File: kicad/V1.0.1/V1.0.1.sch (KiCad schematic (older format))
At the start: 20 parts, among them IC1 OPA2134P, U1 TLE2426CP

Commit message: Started to include libraries and sort out names to link to PCB
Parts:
- IC1: footprint V1.0.1:AKAFUGU_DIL-8 -> V1.0.1:DIL-8; symbol AKAFUGU_OPA2134P -> OPA2134P
- JACK-IN9, JACK-OUT9: footprint V1.0.1:AKAFUGU_STX3100 -> V1.0.1:STX3100; symbol AKAFUGU_STEREOJACK -> STEREOJACK
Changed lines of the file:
@@
 $EndComp
 $Comp
-L AKAFUGU_GND #GND01
+L GND #GND01
 U 1 1 58DE8183
 P 5200 3450
@@
 $EndComp
 $Comp
-L AKAFUGU_GND #GND02
+L GND #GND02
 U 1 1 58DE81E7
 P 5200 4350
@@
 $EndComp
 $Comp
-L AKAFUGU_OPA2134P IC1
+L OPA2134P IC1
 U 1 1 58DE82AF
 P 4600 5350
 F 0 "IC1" H 4700 5575 70  0000 L BNN
 F 1 "OPA2134P" H 4699 5150 70  0000 L BNN
-F 2 "V1.0.1:AKAFUGU_DIL-8" H 4590 5140 65  0001 L TNN
+F 2 "V1.0.1:DIL-8" H 4590 5140 65  0001 L TNN
 F 3 "" H 4600 5350 60  0001 C CNN
 	1    4600 5350
@@
 $EndComp
 $Comp
-L AKAFUGU_OPA2134P IC1
+L OPA2134P IC1
 U 2 1 58DE8313
 P 3200 2150
 F 0 "IC1" H 3300 2375 70  0000 L BNN
 F 1 "OPA2134P" H 3299 1950 70  0000 L BNN
-F 2 "V1.0.1:AKAFUGU_DIL-8" H 3190 1940 65  0001 L TNN
+F 2 "V1.0.1:DIL-8" H 3190 1940 65  0001 L TNN
 F 3 "" H 3200 2150 60  0001 C CNN
 	2    3200 2150
@@
 $EndComp
 $Comp
-L AKAFUGU_STEREOJACK JACK-IN9
+L STEREOJACK JACK-IN9
 U 1 1 58DE83DB
 P 5700 3050
 F 0 "JACK-IN9" H 5400 3200 70  0000 L BNN
 F 1 "STEREOJACK" H 5400 2650 70  0000 L BNN
-F 2 "V1.0.1:AKAFUGU_STX3100" H 5690 2840 65  0001 L TNN
+F 2 "V1.0.1:STX3100" H 5690 2840 65  0001 L TNN
 F 3 "" H 5700 3050 60  0001 C CNN
 	1    5700 3050
@@
 $EndComp
 $Comp
-L AKAFUGU_STEREOJACK JACK-OUT9
+L STEREOJACK JACK-OUT9
 U 1 1 58DE84A3
 P 5700 3950
 F 0 "JACK-OUT9" H 5400 4100 70  0000 L BNN
 F 1 "STEREOJACK" H 5400 3550 70  0000 L BNN
-F 2 "V1.0.1:AKAFUGU_STX3100" H 5690 3740 65  0001 L TNN
+F 2 "V1.0.1:STX3100" H 5690 3740 65  0001 L TNN
 F 3 "" H 5700 3950 60  0001 C CNN
 	1    5700 3950

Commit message: Corrected Schematic errors
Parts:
- renumbered 9V9 to 9V1, C1V+9 to C1V+1, C1V-9 to C1V-1, C4 to C2, C2L9 to C2L1, C2R9 to C2R1, JACK-IN9 to JACK-IN1, JACK-OUT9 to JACK-OUT1, R3L9 to R3L1, R3R9 to R3R1, R4L9 to R4L1, R4R9 to R4R1, R5L9 to R5L1, R5R9 to R5R1, R6L9 to R6L1, R6R9 to R6R1
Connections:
- net labels added: INPUT_L, INPUT_R, OUTPUT_L, OUTPUT_R
- wire segments 45 -> 48
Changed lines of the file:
@@
 EESchema Schematic File Version 2
 LIBS:V1.0.1
-LIBS:V1.0.1-cache
 EELAYER 25 0
 EELAYER END
@@
 Gain = 6
 $Comp
-L BATTERY_AB9V 9V9
+L BATTERY_AB9V 9V1
 U 1 1 58DE7C6F
 P 7950 5550
-F 0 "9V9" H 7725 5675 70  0000 L BNN
+F 0 "9V1" H 7725 5675 70  0000 L BNN
 F 1 "AB9V" H 7725 5350 70  0000 L BNN
 F 2 "V1.0.1:BATTERY_AB9V" H 7725 5350 70  0001 L BNN
@@
 $EndComp
 $Comp
-L CAPACITOR-WIMA_C2.5_2 C1V+9
+L CAPACITOR-WIMA_C2.5_2 C1V+1
 U 1 1 58DE7DFF
 P 10050 5250
-F 0 "C1V+9" H 10110 5265 70  0000 L BNN
+F 0 "C1V+1" H 10110 5265 70  0000 L BNN
 F 1 "0.068uF" H 10110 5065 70  0000 L BNN
 F 2 "V1.0.1:CAPACITOR-WIMA_C2.5-2" H 10040 5040 65  0001 L TNN
@@
 $EndComp
 $Comp
-L CAPACITOR-WIMA_C2.5_2 C1V-9
+L CAPACITOR-WIMA_C2.5_2 C1V-1
 U 1 1 58DE7EC7
 P 10050 5750
-F 0 "C1V-9" H 10110 5765 70  0000 L BNN
+F 0 "C1V-1" H 10110 5765 70  0000 L BNN
 F 1 "0.068uF" H 10110 5565 70  0000 L BNN
 F 2 "V1.0.1:CAPACITOR-WIMA_C2.5-2" H 10040 5540 65  0001 L TNN
@@
 $EndComp
 $Comp
-L CAPACITOR-WIMA_C5_5 C2L9
+L CAPACITOR-WIMA_C5_5 C2L1
 U 1 1 58DE7F8F
 P 4300 2050
-F 0 "C2L9" H 4360 2065 70  0000 L BNN
+F 0 "C2L1" H 4360 2065 70  0000 L BNN
 F 1 "0.1uF" H 4360 1865 70  0000 L BNN
 F 2 "V1.0.1:CAPACITOR-WIMA_C5B5" H 4290 1840 65  0001 L TNN
@@
 $EndComp
 $Comp
-L CAPACITOR-WIMA_C5_5 C2R9
+L CAPACITOR-WIMA_C5_5 C2R1
 U 1 1 58DE8057
 P 3500 5250
-F 0 "C2R9" H 3560 5265 70  0000 L BNN
+F 0 "C2R1" H 3560 5265 70  0000 L BNN
 F 1 "0.1uF" H 3560 5065 70  0000 L BNN
 F 2 "V1.0.1:CAPACITOR-WIMA_C5B5" H 3490 5040 65  0001 L TNN
@@
 $EndComp
 $Comp
-L CAPACITOR-WIMA_C5_2.5 C4
+L CAPACITOR-WIMA_C5_2.5 C2
 U 1 1 58DE811F
 P 9650 5850
-F 0 "C4" H 9710 5864 70  0000 L BNN
+F 0 "C2" H 9710 5864 70  0000 L BNN
 F 1 "1uF" H 9709 5665 70  0000 L BNN
 F 2 "V1.0.1:CAPACITOR-WIMA_C5B2.5" H 9640 5640 65  0001 L TNN
 F 3 "" H 9650 5850 60  0001 C CNN
 	1    9650 5850
-	1    0    0    -1
-$EndComp
-$Comp
-L GND #GND01
-U 1 1 58DE8183
-P 5200 3450
-F 0 "#GND01" H 5100 3350 70  0001 L BNN
-F 1 "GND" H 5100 3350 70  0000 L BNN
-F 2 "" H 5200 3450 60  0001 C CNN
-F 3 "" H 5200 3450 60  0001 C CNN
-	1    5200 3450
-	1    0    0    -1
-$EndComp
-$Comp
-L GND #GND02
-U 1 1 58DE81E7
-P 5200 4350
-F 0 "#GND02" H 5100 4250 70  0001 L BNN
-F 1 "GND" H 5100 4250 70  0000 L BNN
-F 2 "" H 5200 4350 60  0001 C CNN
-F 3 "" H 5200 4350 60  0001 C CNN
-	1    5200 4350
 	1    0    0    -1
 $EndComp
@@
 $EndComp
 $Comp
-L STEREOJACK JACK-IN9
+L STEREOJACK JACK-IN1
 U 1 1 58DE83DB
 P 5700 3050
-F 0 "JACK-IN9" H 5400 3200 70  0000 L BNN
+F 0 "JACK-IN1" H 5400 3200 70  0000 L BNN
 F 1 "STEREOJACK" H 5400 2650 70  0000 L BNN
 F 2 "V1.0.1:STX3100" H 5690 2840 65  0001 L TNN
@@
 $EndComp
 $Comp
-L STEREOJACK JACK-OUT9
+L STEREOJACK JACK-OUT1
 U 1 1 58DE84A3
 P 5700 3950
-F 0 "JACK-OUT9" H 5400 4100 70  0000 L BNN
+F 0 "JACK-OUT1" H 5400 4100 70  0000 L BNN
 F 1 "STEREOJACK" H 5400 3550 70  0000 L BNN
 F 2 "V1.0.1:STX3100" H 5690 3740 65  0001 L TNN
@@
 $EndComp
 $Comp
-L SUPPLY1_V+ #P+03
+L SUPPLY1_V+ #P+2
 U 1 1 58DE8507
 P 4500 4950
-F 0 "#P+03" V 4400 4850 70  0001 L BNN
+F 0 "#P+2" V 4400 4850 70  0001 L BNN
 F 1 "V+" V 4400 4850 70  0000 L BNN
 F 2 "" H 4500 4950 60  0001 C CNN
@@
 $EndComp
 $Comp
-L SUPPLY1_V+ #P+04
+L SUPPLY1_V+ #P+1
 U 1 1 58DE856B
 P 10150 4850
-F 0 "#P+04" V 10050 4750 70  0001 L BNN
+F 0 "#P+1" V 10050 4750 70  0001 L BNN
 F 1 "V+" V 10050 4750 70  0000 L BNN
 F 2 "" H 10150 4850 60  0001 C CNN
@@
 $EndComp
 $Comp
-L SUPPLY1_V- #P-05
+L SUPPLY1_V- #P-1
 U 1 1 58DE85CF
 P 4500 5750
-F 0 "#P-05" V 4300 5850 70  0001 R TNN
+F 0 "#P-1" V 4300 5850 70  0001 R TNN
 F 1 "V-" V 4300 5850 70  0000 R TNN
 F 2 "" H 4500 5750 60  0001 C CNN
@@
 $EndComp
 $Comp
-L SUPPLY1_V- #P-06
+L SUPPLY1_V- #P-2
 U 1 1 58DE8633
 P 10150 6250
-F 0 "#P-06" V 9950 6350 70  0001 R TNN
+F 0 "#P-2" V 9950 6350 70  0001 R TNN
 F 1 "V-" V 9950 6350 70  0000 R TNN
 F 2 "" H 10150 6250 60  0001 C CNN
@@
 $EndComp
 $Comp
-L RESISTOR_R-EU_0207_2V R3L9
+L RESISTOR_R-EU_0207_2V R3L1
 U 1 1 58DE86FB
 P 3900 2350
-F 0 "R3L9" H 3750 2409 70  0000 L BNN
+F 0 "R3L1" H 3750 2409 70  0000 L BNN
 F 1 "100k" H 3750 2220 70  0000 L BNN
 F 2 "V1.0.1:RESISTOR_0207_2V" H 3890 2140 65  0001 L TNN
@@
 $EndComp
 $Comp
-L RESISTOR_R-EU_0207_2V R3R9
+L RESISTOR_R-EU_0207_2V R3R1
 U 1 1 58DE87C3
 P 3900 5550
-F 0 "R3R9" H 3750 5609 70  0000 L BNN
+F 0 "R3R1" H 3750 5609 70  0000 L BNN
 F 1 "100k" H 3750 5420 70  0000 L BNN
 F 2 "V1.0.1:RESISTOR_0207_2V" H 3890 5340 65  0001 L TNN
@@
 $EndComp
 $Comp
-L RESISTOR_R-EU_0207_2V R4L9
+L RESISTOR_R-EU_0207_2V R4L1
 U 1 1 58DE888B
 P 3600 3150
-F 0 "R4L9" H 3450 3209 70  0000 L BNN
+F 0 "R4L1" H 3450 3209 70  0000 L BNN
 F 1 "2k" H 3450 3020 70  0000 L BNN
 F 2 "V1.0.1:RESISTOR_0207_2V" H 3590 2940 65  0001 L TNN
@@
 $EndComp
 $Comp
-L RESISTOR_R-EU_0207_2V R4R9
+L RESISTOR_R-EU_0207_2V R4R1
 U 1 1 58DE8953
 P 4200 6350
-F 0 "R4R9" H 4050 6409 70  0000 L BNN
+F 0 "R4R1" H 4050 6409 70  0000 L BNN
 F 1 "2k" H 4050 6220 70  0000 L BNN
 F 2 "V1.0.1:RESISTOR_0207_2V" H 4190 6140 65  0001 L TNN
@@
 $EndComp
 $Comp
-L RESISTOR_R-EU_0207_2V R5L9
+L RESISTOR_R-EU_0207_2V R5L1
 U 1 1 58DE8A1B
 P 2600 2150
-F 0 "R5L9" H 2450 2208 70  0000 L BNN
+F 0 "R5L1" H 2450 2208 70  0000 L BNN
 F 1 "47R" H 2450 2020 70  0000 L BNN
 F 2 "V1.0.1:RESISTOR_0207_2V" H 2590 1940 65  0001 L TNN
@@
 $EndComp
 $Comp
-L RESISTOR_R-EU_0207_2V R5R9
+L RESISTOR_R-EU_0207_2V R5R1
 U 1 1 58DE8AE3
 P 5200 5350
-F 0 "R5R9" H 5050 5408 70  0000 L BNN
+F 0 "R5R1" H 5050 5408 70  0000 L BNN
 F 1 "47R" H 5050 5220 70  0000 L BNN
 F 2 "V1.0.1:RESISTOR_0207_2V" H 5190 5140 65  0001 L TNN
@@
 $EndComp
 $Comp
-L RESISTOR_R-EU_0207_2V R6L9
+L RESISTOR_R-EU_0207_2V R6L1
 U 1 1 58DE8BAB
 P 2900 2850
-F 0 "R6L9" H 2750 2908 70  0000 L BNN
+F 0 "R6L1" H 2750 2908 70  0000 L BNN
 F 1 "10k" H 2750 2720 70  0000 L BNN
 F 2 "V1.0.1:RESISTOR_0207_2V" H 2890 2640 65  0001 L TNN
@@
 $EndComp
 $Comp
-L RESISTOR_R-EU_0207_2V R6R9
+L RESISTOR_R-EU_0207_2V R6R1
 U 1 1 58DE8C73
 P 4900 6050
-F 0 "R6R9" H 4750 6108 70  0000 L BNN
+F 0 "R6R1" H 4750 6108 70  0000 L BNN
 F 1 "10k" H 4750 5920 70  0000 L BNN
 F 2 "V1.0.1:RESISTOR_0207_2V" H 4890 5840 65  0001 L TNN
@@
 $EndComp
 $Comp
-L SUPPLY2_GND #SUPPLY07
+L SUPPLY2_GND #SUPPLY1
 U 1 1 58DE8CD7
 P 5000 2550
-F 0 "#SUPPLY07" H 4925 2425 70  0001 L BNN
+F 0 "#SUPPLY1" H 4925 2425 70  0001 L BNN
 F 1 "GND" H 4925 2425 70  0000 L BNN
 F 2 "" H 5000 2550 60  0001 C CNN
@@
 $EndComp
 $Comp
-L SUPPLY2_GND #SUPPLY08
+L SUPPLY2_GND #SUPPLY2
 U 1 1 58DE8D3B
 P 3900 2750
-F 0 "#SUPPLY08" H 3825 2625 70  0001 L BNN
+F 0 "#SUPPLY2" H 3825 2625 70  0001 L BNN
 F 1 "GND" H 3825 2625 70  0000 L BNN
 F 2 "" H 3900 2750 60  0001 C CNN
@@
 $EndComp
 $Comp
-L SUPPLY2_GND #SUPPLY09
+L SUPPLY2_GND #SUPPLY3
 U 1 1 58DE8D9F
 P 3600 3550
-F 0 "#SUPPLY09" H 3525 3425 70  0001 L BNN
+F 0 "#SUPPLY3" H 3525 3425 70  0001 L BNN
 F 1 "GND" H 3525 3425 70  0000 L BNN
 F 2 "" H 3600 3550 60  0001 C CNN
@@
 $EndComp
 $Comp
-L SUPPLY2_GND #SUPPLY010
+L SUPPLY2_GND #SUPPLY5
 U 1 1 58DE8E03
 P 2800 5750
-F 0 "#SUPPLY010" H 2725 5625 70  0001 L BNN
+F 0 "#SUPPLY5" H 2725 5625 70  0001 L BNN
 F 1 "GND" H 2725 5625 70  0000 L BNN
 F 2 "" H 2800 5750 60  0001 C CNN
@@
 $EndComp
 $Comp
-L SUPPLY2_GND #SUPPLY011
+L SUPPLY2_GND #SUPPLY6
 U 1 1 58DE8E67
 P 3900 5950
-F 0 "#SUPPLY011" H 3825 5825 70  0001 L BNN
+F 0 "#SUPPLY6" H 3825 5825 70  0001 L BNN
 F 1 "GND" H 3825 5825 70  0000 L BNN
 F 2 "" H 3900 5950 60  0001 C CNN
@@
 $EndComp
 $Comp
-L SUPPLY2_GND #SUPPLY012
+L SUPPLY2_GND #SUPPLY7
 U 1 1 58DE8ECB
 P 4200 6750
-F 0 "#SUPPLY012" H 4125 6625 70  0001 L BNN
+F 0 "#SUPPLY7" H 4125 6625 70  0001 L BNN
 F 1 "GND" H 4125 6625 70  0000 L BNN
 F 2 "" H 4200 6750 60  0001 C CNN
@@
 $EndComp
 $Comp
-L SUPPLY2_GND #SUPPLY013
+L SUPPLY2_GND #SUPPLY4
 U 1 1 58DE8F2F
 P 10250 5550
-F 0 "#SUPPLY013" H 10175 5425 70  0001 L BNN
+F 0 "#SUPPLY4" H 10175 5425 70  0001 L BNN
 F 1 "GND" H 10175 5425 70  0000 L BNN
 F 2 "" H 10250 5550 60  0001 C CNN
@@
 	5100 6050 5500 6050
 Wire Wire Line
-	5400 5350 6000 5350
+	5400 5350 6025 5350
 Wire Wire Line
 	5500 6050 5500 5350
@@
 Text Label 3300 5250 2    10   ~ 0
 VOLUME-OUT-R
+Text GLabel 1800 2150 0    60   Input ~ 0
+OUTPUT_L
+Text GLabel 4800 1050 0    60   Input ~ 0
+INPUT_L
+Text GLabel 4600 3250 0    60   Input ~ 0
+INPUT_L
+Text GLabel 4600 2950 0    60   Input ~ 0
+INPUT_R
+Text GLabel 2650 4250 0    60   Input ~ 0
+INPUT_R
+Text GLabel 6025 5350 2    60   Input ~ 0
+OUTPUT_R
+Wire Wire Line
+	2650 4250 2800 4250
+Wire Wire Line
+	5000 1050 4800 1050
+Text GLabel 4600 3850 0    60   Input ~ 0
+OUTPUT_R
+Text GLabel 4600 4150 0    60   Input ~ 0
+OUTPUT_L
+$Comp
+L SUPPLY2_GND #SUPPLY?
+U 1 1 58DEC8E3
+P 5200 3450
+F 0 "#SUPPLY?" H 5125 3325 70  0001 L BNN
+F 1 "GND" H 5125 3325 70  0000 L BNN
+F 2 "" H 5200 3450 60  0001 C CNN
+F 3 "" H 5200 3450 60  0001 C CNN
+	1    5200 3450
+	1    0    0    -1
+$EndComp
+$Comp
+L SUPPLY2_GND #SUPPLY?
+U 1 1 58DEC930
+P 5175 4350
+F 0 "#SUPPLY?" H 5100 4225 70  0001 L BNN
+F 1 "GND" H 5100 4225 70  0000 L BNN
+F 2 "" H 5175 4350 60  0001 C CNN
+F 3 "" H 5175 4350 60  0001 C CNN
+	1    5175 4350
+	1    0    0    -1
+$EndComp
+Wire Wire Line
+	5200 4250 5175 4250
 $EndSCHEMATC

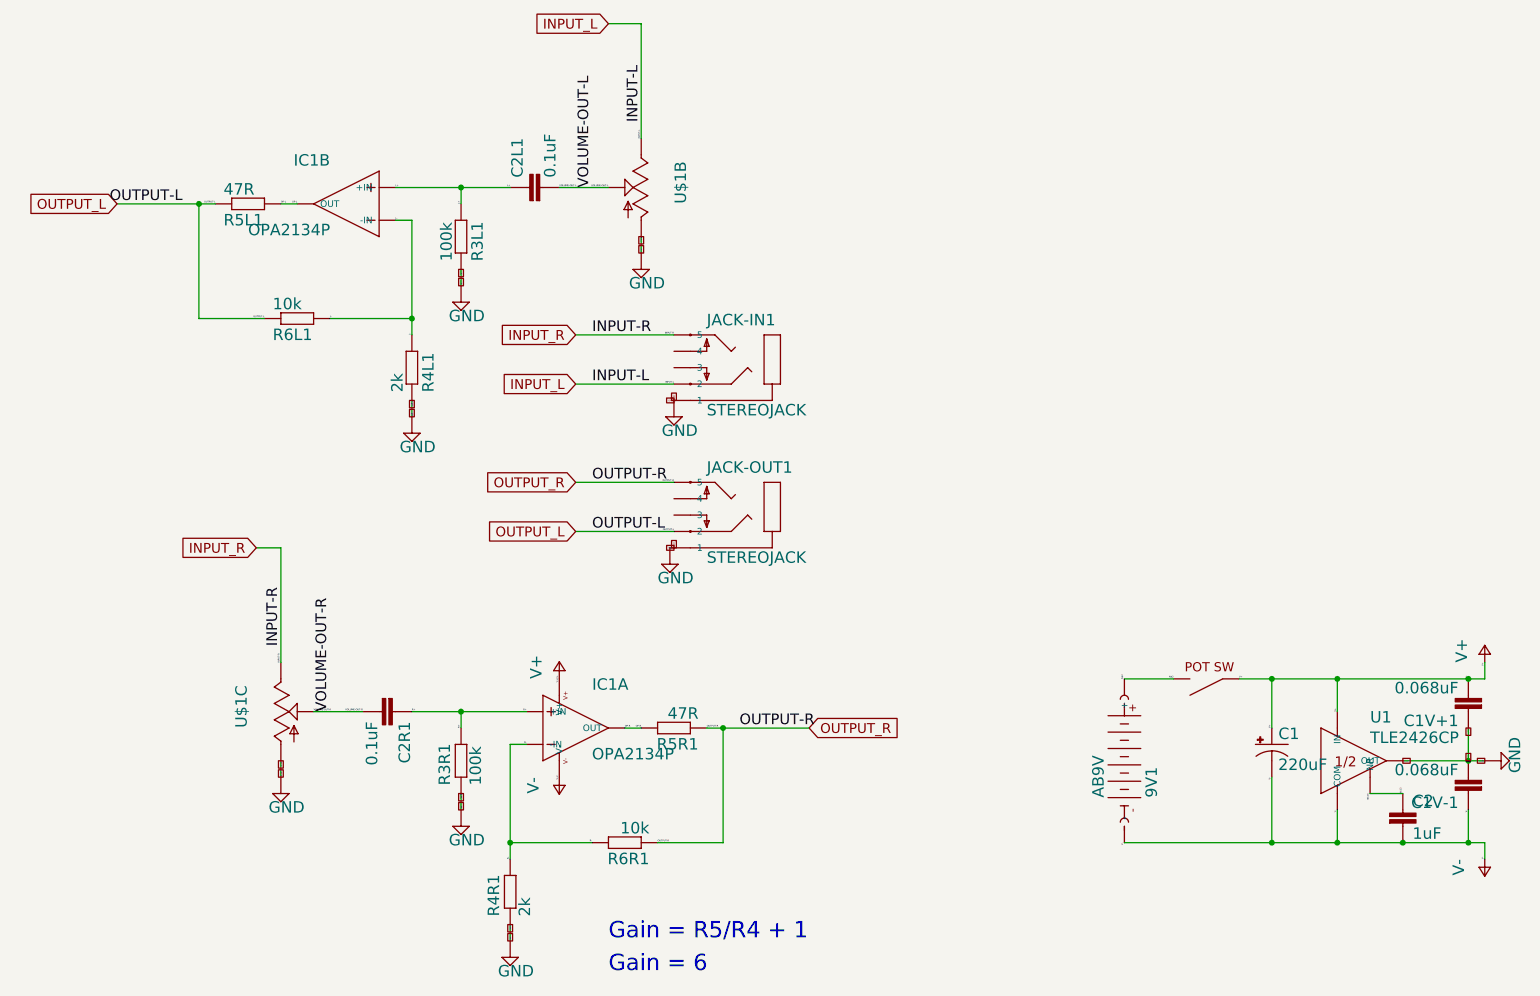
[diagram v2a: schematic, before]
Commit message: Corrected conversion errors
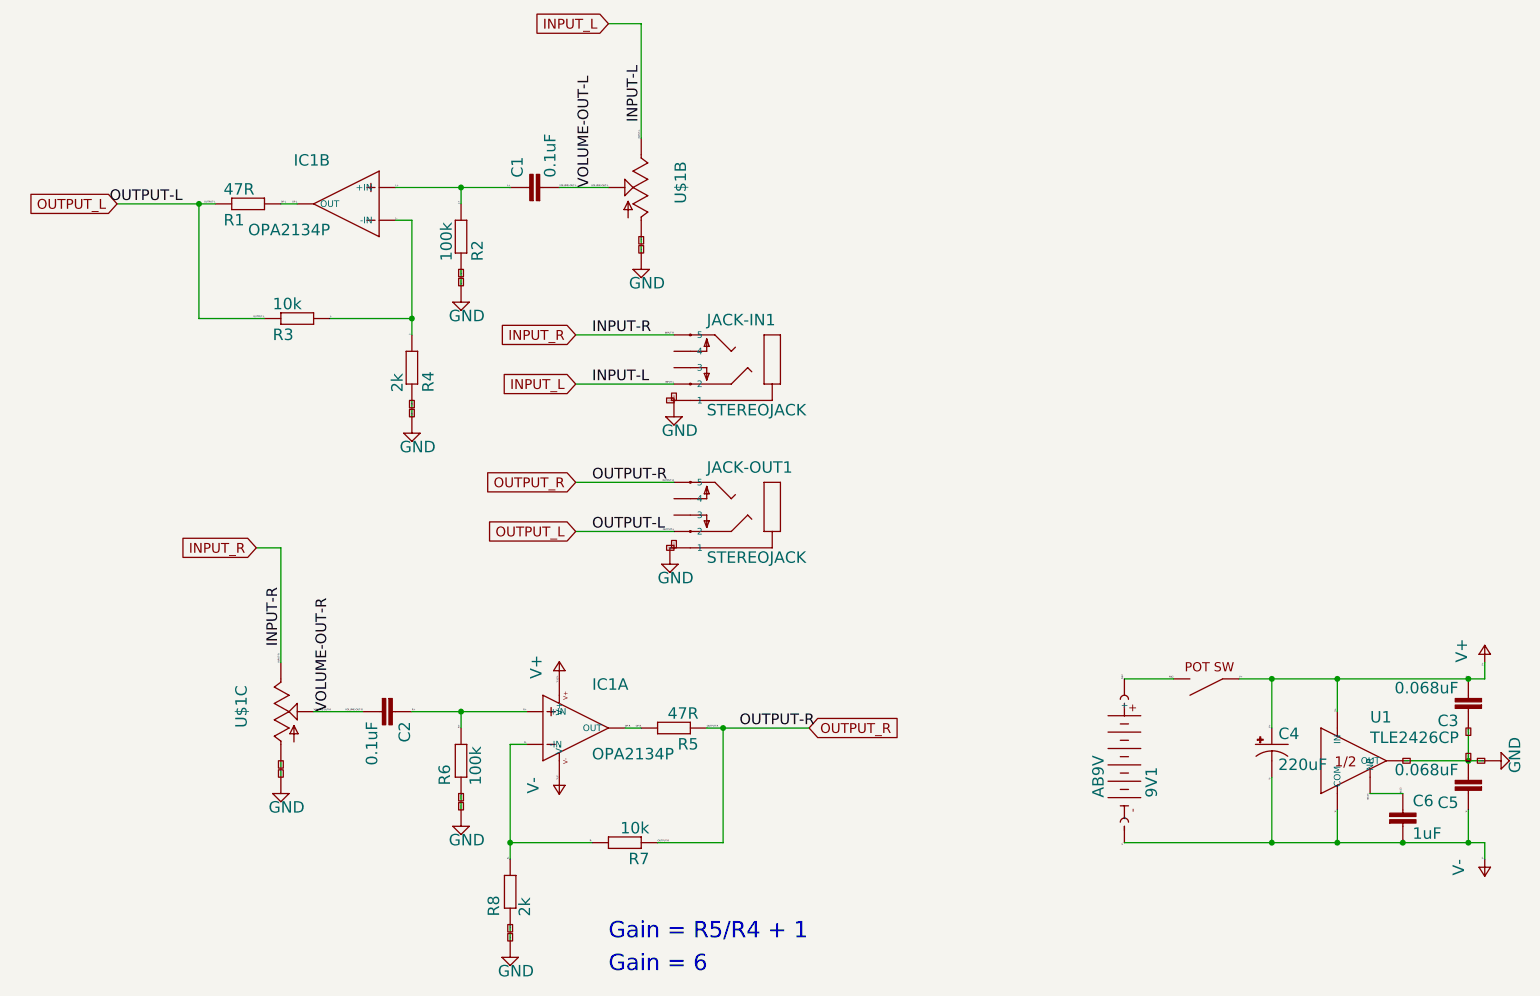
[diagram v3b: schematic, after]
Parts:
- 9V1: footprint V1.0.1:BATTERY_AB9V -> CMOY:BATTERY_AB9V
- C1: renamed from C2L1; footprint V1.0.1:CAPACITOR-WIMA_C5B5 -> CMOY:CAPACITOR-WIMA_C5B5
- C2: renamed from C2R1; footprint V1.0.1:CAPACITOR-WIMA_C5B5 -> CMOY:CAPACITOR-WIMA_C5B5
- C3: renamed from C1V+1; footprint V1.0.1:CAPACITOR-WIMA_C2.5-2 -> CMOY:CAPACITOR-WIMA_C2.5-2
- C4: renamed from C1; footprint V1.0.1:RCL_E3_5-8 -> CMOY:RCL_E3_5-8
- C5: renamed from C1V-1; footprint V1.0.1:CAPACITOR-WIMA_C2.5-2 -> CMOY:CAPACITOR-WIMA_C2.5-2
- C6: renamed from C2; footprint V1.0.1:CAPACITOR-WIMA_C5B2.5 -> CMOY:CAPACITOR-WIMA_C5B2.5
- IC1: footprint V1.0.1:DIL-8 -> CMOY:DIL-8
- JACK-IN1, JACK-OUT1: footprint V1.0.1:STX3100 -> CMOY:STX3100
- R1: renamed from R5L1; footprint V1.0.1:RESISTOR_0207_2V -> CMOY:RESISTOR_0207_2V
- R2: renamed from R3L1; footprint V1.0.1:RESISTOR_0207_2V -> CMOY:RESISTOR_0207_2V
- R3: renamed from R6L1; footprint V1.0.1:RESISTOR_0207_2V -> CMOY:RESISTOR_0207_2V
- R4: renamed from R4L1; footprint V1.0.1:RESISTOR_0207_2V -> CMOY:RESISTOR_0207_2V
- R5: renamed from R5R1; footprint V1.0.1:RESISTOR_0207_2V -> CMOY:RESISTOR_0207_2V
- R6: renamed from R3R1; footprint V1.0.1:RESISTOR_0207_2V -> CMOY:RESISTOR_0207_2V
- R7: renamed from R6R1; footprint V1.0.1:RESISTOR_0207_2V -> CMOY:RESISTOR_0207_2V
- R8: renamed from R4R1; footprint V1.0.1:RESISTOR_0207_2V -> CMOY:RESISTOR_0207_2V
- U$1: footprint V1.0.1:AUDIO-POTS_ALPS_RK0971221Z0X -> CMOY:AUDIO-POTS_ALPS_RK0971221Z0X
- U1: footprint V1.0.1:TLE2426_DIP-8 -> CMOY:TLE2426_DIP-8
